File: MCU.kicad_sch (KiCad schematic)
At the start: 34 parts, among them J7 Conn_01x04, J8 PinHeader_2x5_P1.27mm_SMD, SW1 SW_KSC441J70SHLFS_SMD, SW2 SW_KSC441J70SHLFS_SMD, U3 STM32U585CIT3, Y1 Oscillator_40MHz_YIC_OSC-S5

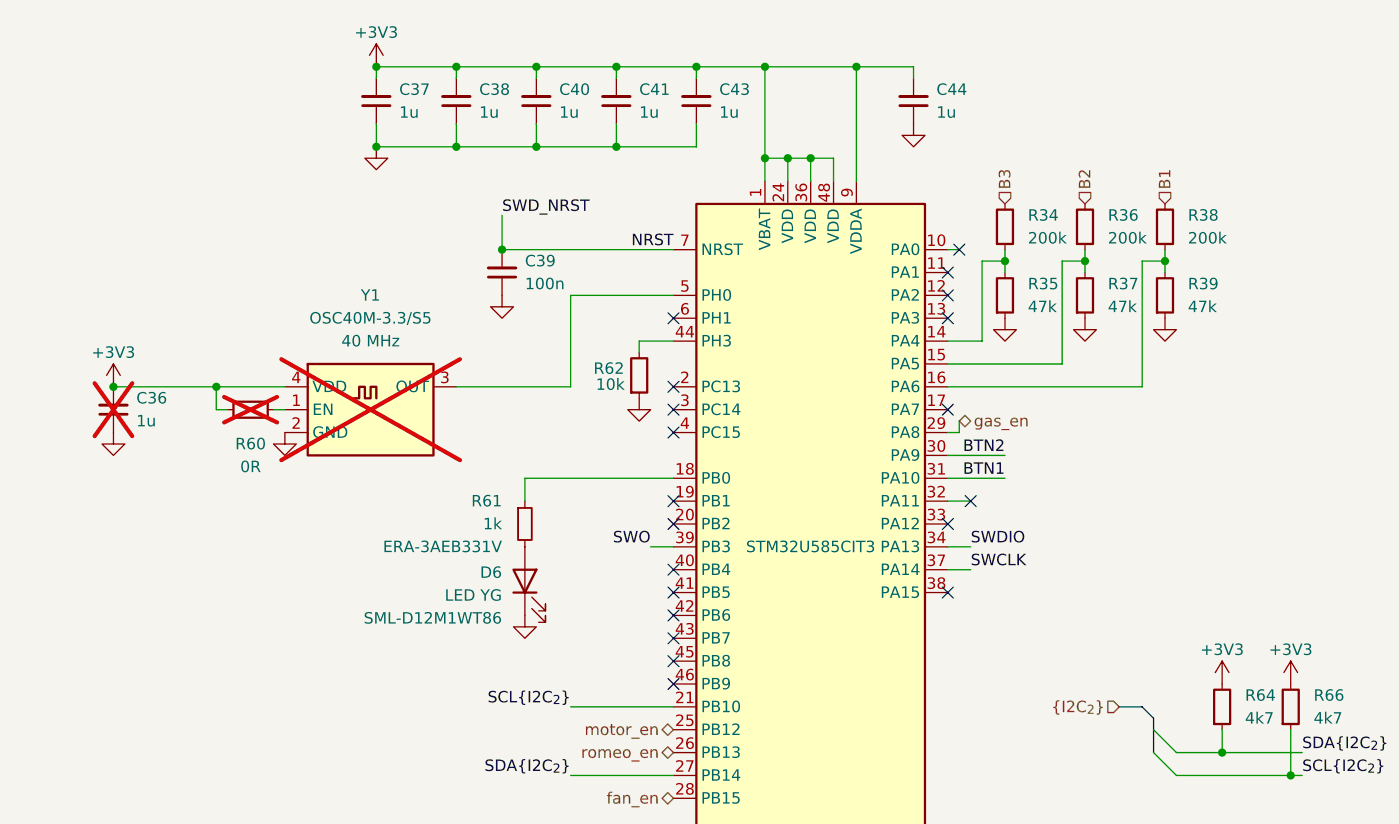
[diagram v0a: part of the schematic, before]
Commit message: Added B1 B2 B3 resistors footprints and traces
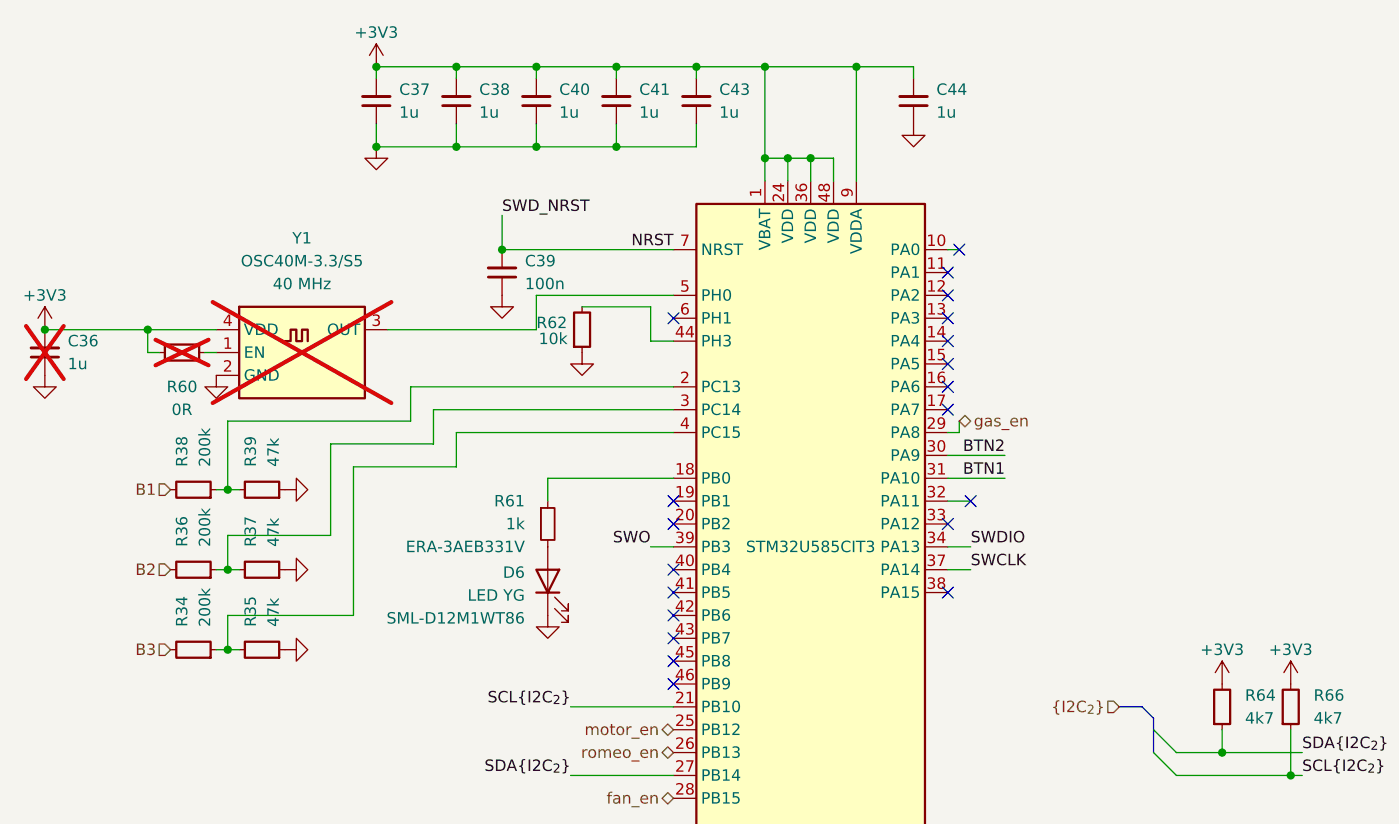
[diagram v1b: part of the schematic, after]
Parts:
- R34, R35, R36, R37, R38, R39: footprint Hardware Components Footprints:R_0402_1005Metric -> Resistor_SMD:R_0402_1005Metric
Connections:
- net at R34.1, R35.2: now also U3.4 (PC15); no longer U3.14 (PA4)
- net at R38.1, R39.2: now also U3.2 (PC13); no longer U3.16 (PA6)
- net at R36.1, R37.2: now also U3.3 (PC14); no longer U3.15 (PA5)
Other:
- moved on the sheet: C36, D6, R34, R35, R36, R37, R38, R39, R60, R61, R62, Y1

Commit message: fixes and stuff
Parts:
- added C22, C23, C24, C25: C_100n_50V_X8L_0402, Hardware Components Footprints:C_0402_1005Metric, symbol lib:C_100n_50V_X8L_0402
- added R34: R_47k_0402, Resistor_SMD:R_0402_1005Metric, symbol Hardware Components:R_47k_0402
- added R8: R_200k_0402, Resistor_SMD:R_0402_1005Metric, symbol Hardware Components:R_200k_0402
- renumbered R34 to R35, R35 to R36, R36 to R37, R37 to R38, R38 to R39, R39 to R41
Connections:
- net GND: now also C22.1, C23.1, C24.1, C25.1, R34.1
- net at R35.1, R36.2: now also U3.13 (PA3), C24.2; no longer U3.4 (PC15)
- net at R39.1, R41.2: now also U3.15 (PA5), C22.2; no longer U3.2 (PC13)
- net at R37.1, R38.2: now also U3.14 (PA4), C23.2; no longer U3.3 (PC14)
- net at U3.16 (PA6): now also C25.2, R34.2, R8.1
- new net +16V: R8.2
- no-connect marks 22 -> 21
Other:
- moved on the sheet: R35, R36, R37, R38, R39, R41

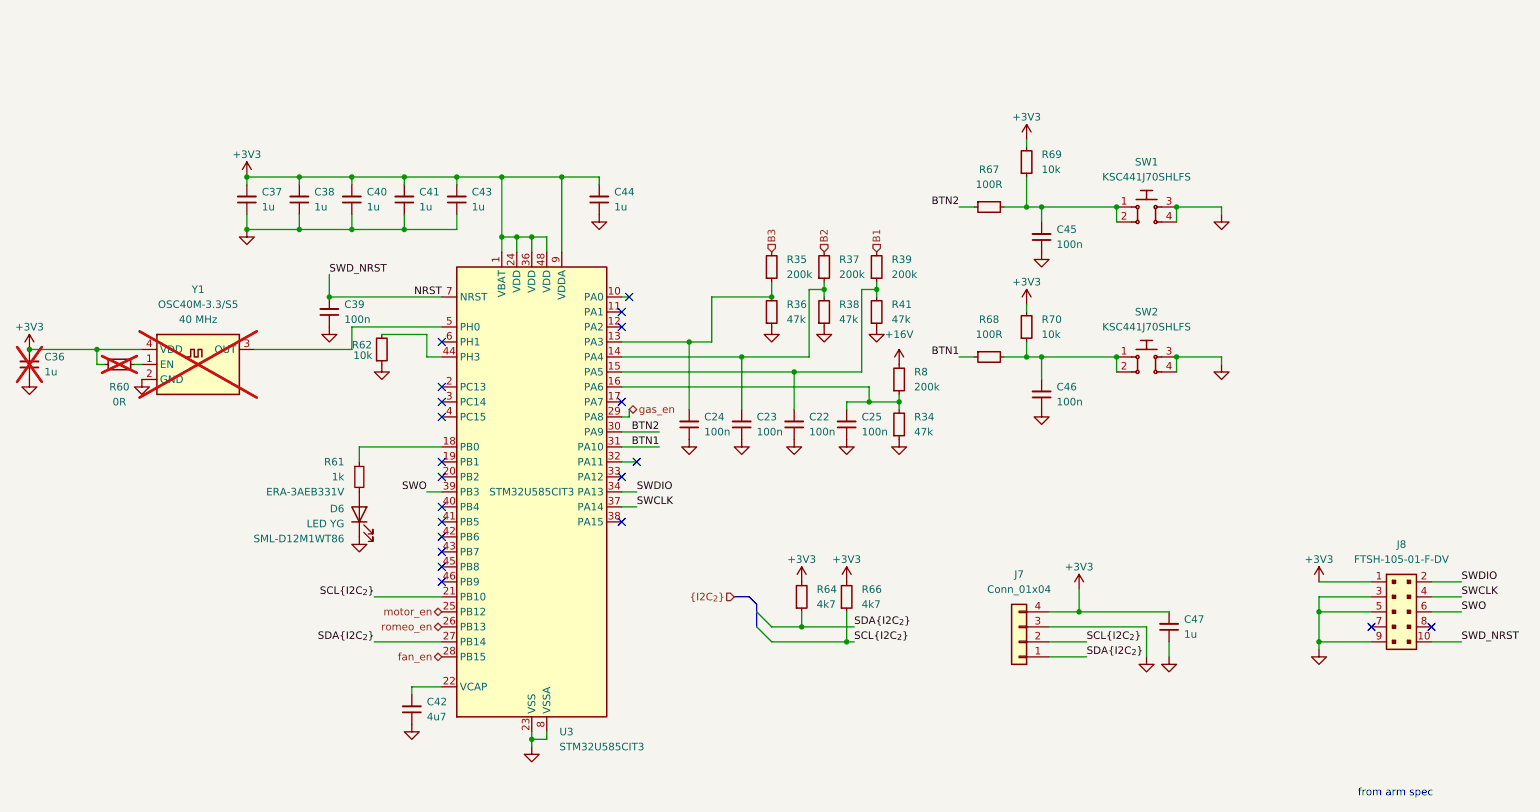
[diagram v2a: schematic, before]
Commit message: Adjustable output
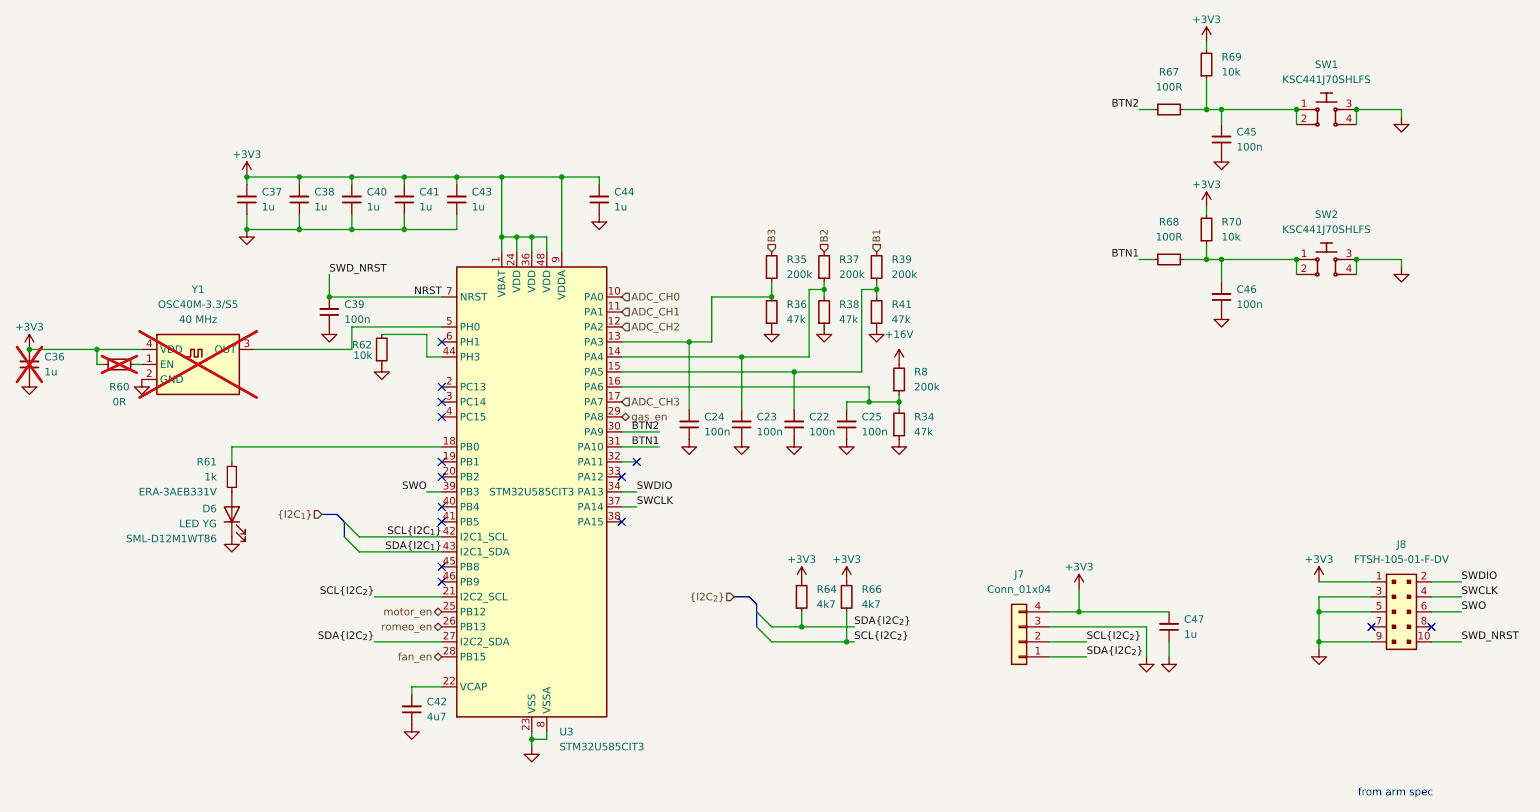
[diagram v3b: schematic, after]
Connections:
- net ADC_CH0: now reaches U3.10 (PA0)
- net ADC_CH1: now reaches U3.11 (PA1)
- net ADC_CH2: now reaches U3.12 (PA2)
- net ADC_CH3: now reaches U3.17 (PA7)
- net SCL{I2C_{1}}: now reaches U3.42 (PB6)
- net SDA{I2C_{1}}: now reaches U3.43 (PB7)
- no-connect marks 21 -> 15
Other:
- moved on the sheet: C45, C46, D6, R61, R67, R69, R70, SW1, SW2

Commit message: test points
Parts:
- added TP30, TP31, TP32, TP33, TP34, TP35, TP36: TP_2.54mm_THT_5002, Hardware Components Footprints:TP_2.54mm_THT_Keystone_500x, symbol Hardware Components:TP_2.54mm_THT_5002
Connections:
- net +3V3: now also TP32.1
- net BTN1: now also TP31.1
- net BTN2: now also TP30.1
- net at C23.2, R37.1, R38.2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: now also TP34.1
- net at C24.2, R35.1, R36.2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: now also TP33.1
- net at C25.2, R34.2, R8.1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: now also TP36.1
- net at C22.2, R39.1, R41.2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: now also TP35.1
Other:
- moved on the sheet: C22, C23, C24, C25, R34, R35, R36, R37, R38, R39, R41, R8
